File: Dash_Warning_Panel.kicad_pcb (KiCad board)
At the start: 2 copper layers, 60 x 40 mm, 30 parts, among them J1 Conn_01x06_Male, SW1 SW_DIP_x02, U1 BD2808MUV, U2 TPS22810-Q1

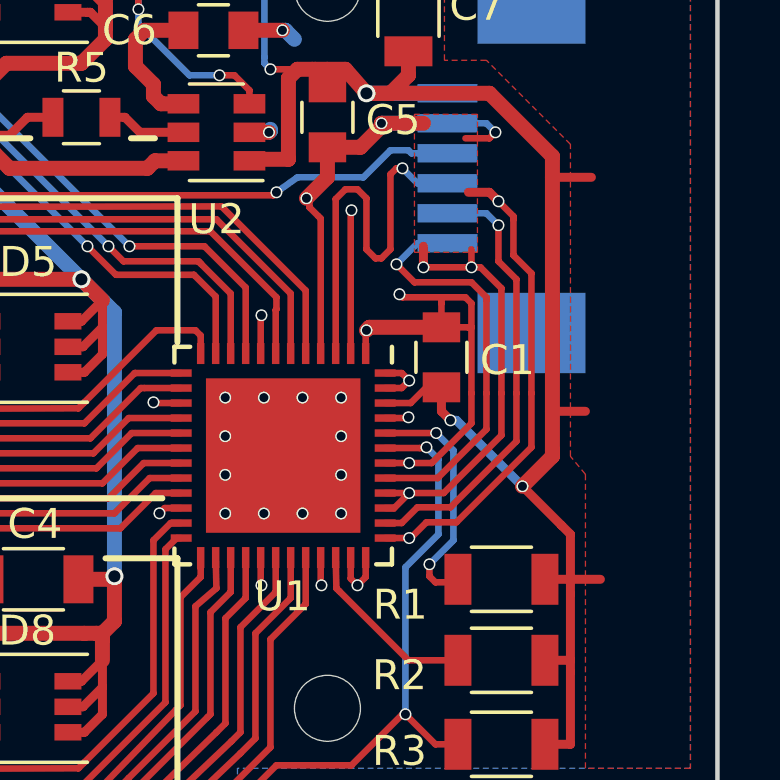
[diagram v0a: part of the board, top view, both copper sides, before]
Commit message: Fixed I2C
Address is 01111000
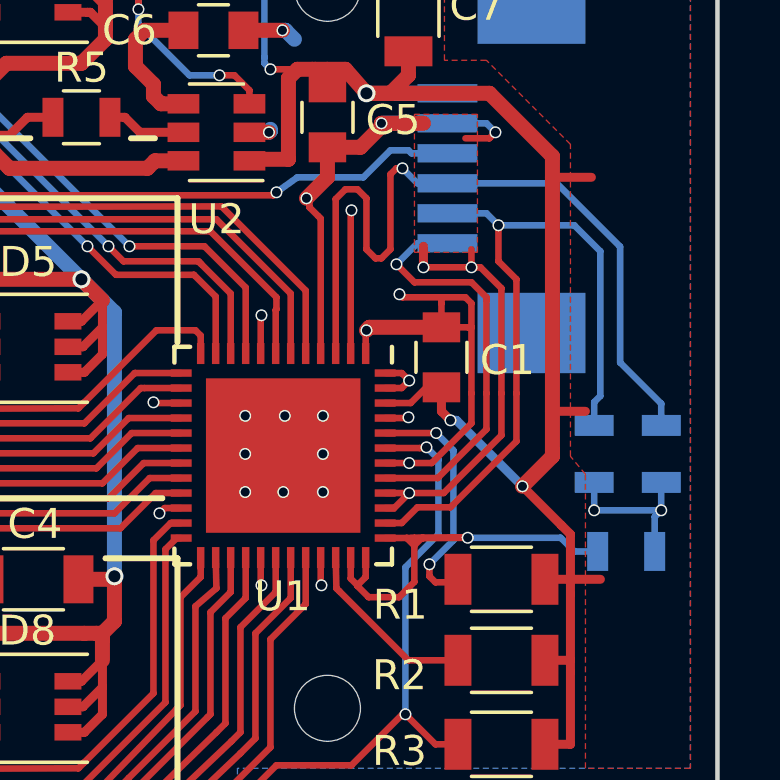
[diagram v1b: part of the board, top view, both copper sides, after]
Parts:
- added R7: 1.8k, Resistors_SMD:R_0805, B.Cu at (226.0, 134.8)
- added R8: 1.8k, Resistors_SMD:R_0805, B.Cu at (227.1, 131.5)
- added R9: 1.8k, Resistors_SMD:R_0805, B.Cu at (224.9, 131.5)
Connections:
- J1 pad : /GND -> (no net)
- U1 pad 35: /GND -> Net-(R7-Pad1)
- U1 pad 36: /GND -> Net-(R7-Pad1)
- U1 pad 37: /GND -> Net-(R7-Pad1)
- U1 pad 49: /GND -> (no net)
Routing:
- net /GND: track 83.9 -> 65.7 mm, vias 38 -> 23
- net Net-(R7-Pad1): track 0.00 -> 15.7 mm, vias 0 -> 1
- net /SDO: track 13.9 -> 27.0 mm
- net /SDI: track 14.8 -> 24.5 mm
- net /VCC: track 58.1 -> 63.6 mm, vias 5 -> 7
- net (no net): vias 0 -> 8
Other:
- board text added: "VCC GND MC SDO SDI CLK"

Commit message: LP5024
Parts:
- removed R2: 68k, Resistors_SMD:R_1206
- added C8: 1uF, Capacitors_SMD:C_0805, F.Cu at (219.2, 131.4)
- R1: value 68k -> 2.45k
- R7, R8, R9: moved to F.Cu
- REF** (x4): value 2.2mm_M2 -> MountingHole_2.2mm_M2
- U1: value BD2808MUV -> LP5024; footprint Housings_DFN_QFN:QFN-48-1EP_7x7mm_Pitch0.5mm -> TI_Additions:VQFN-32-1EP_4x4mm_Pitch0.4mm
- moved R3 4.77 mm to (219.2, 137.2)
- moved R1 4.00 mm to (221.7, 131.7), turned to 270 degrees
- moved C1 3.69 mm to (217.4, 125.5), turned to 270 degrees
- moved U1 1.58 mm to (214.7, 130.0)
- turned R8 to 90 degrees
- turned R9 to 90 degrees
- turned REF** to 0 degrees
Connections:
- C1 pad 1: /VCC -> /GND
- C1 pad 2: /GND -> Net-(C1-Pad2)
- J1 pad 1: /VCC -> /CLK
- J1 pad 2: /GND -> /SDI
- J1 pad 3: /MC -> /SDO
- J1 pad 4: /SDO -> /MC
- J1 pad 5: /SDI -> /GND
- J1 pad 6: /CLK -> /VCC
- R1 pad 2: /VCC -> /GND
- R8 pad 1: /SDO -> /CLK
- U1 pad 1: /GND -> /R0
- U1 pad 10: /G1 -> /R3
- U1 pad 11: /B1 -> /G3
- U1 pad 12: /R2 -> /B3
- U1 pad 13: /G2 -> /R4
- U1 pad 14: /B2 -> /G4
- U1 pad 15: /GND -> /B4
- U1 pad 16: /R3 -> /R5
- U1 pad 17: /G3 -> /G5
- U1 pad 18: /B3 -> /B5
- U1 pad 19: /R4 -> /R6
- U1 pad 2: /GND -> /G0
- U1 pad 20: /G4 -> /G6
- U1 pad 21: /B4 -> /B6
- U1 pad 22: /GND -> /R7
- U1 pad 23: /R5 -> /G7
- U1 pad 24: /G5 -> /B7
- U1 pad 25: /B5 -> Net-(R7-Pad1)
- U1 pad 26: /R6 -> Net-(R7-Pad1)
- U1 pad 27: /G6 -> /VCC
- U1 pad 28: /B6 -> /SDI
- U1 pad 29: /GND -> /CLK
- U1 pad 3: /SDO -> /B0
- U1 pad 30: /R7 -> /OE
- U1 pad 31: /G7 -> Net-(R1-Pad1)
- U1 pad 32: /B7 -> Net-(C1-Pad2)
- U1 pad 4: /GND -> /R1
- U1 pad 5: /R0 -> /G1
- U1 pad 6: /G0 -> /B1
- U1 pad 7: /B0 -> /R2
- U1 pad 8: /GND -> /G2
- U1 pad 9: /R1 -> /B2
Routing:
- net /VCC: track 63.6 -> 0.55 mm, vias 7 -> 0
- net /GND: track 65.7 -> 3.94 mm, vias 23 -> 4
- net /SDO: track 27.0 -> 0.00 mm, vias 1 -> 0
- net /SDI: track 24.5 -> 0.55 mm, vias 1 -> 0
- net Net-(R7-Pad1): track 15.7 -> 1.10 mm, vias 1 -> 0
- net /CLK: track 13.9 -> 0.55 mm, vias 1 -> 0
- net /OE: track 85.5 -> 74.2 mm, vias 3 -> 1
- net Net-(R1-Pad1): track 8.12 -> 0.55 mm, vias 2 -> 0
- net /MC: track 38.7 -> 32.4 mm
- net Net-(R2-Pad2): track 6.07 -> 0.00 mm
- net /G2: track 35.2 -> 39.6 mm
- net /G6: track 31.7 -> 35.5 mm
- net /R6: track 30.8 -> 34.5 mm
- net /B6: track 35.9 -> 39.5 mm
- net /B5: track 44.3 -> 47.8 mm
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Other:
- net class Default: clearance 0.15 -> 0.18
- rule trace_clearance: 0.15 -> 0.18
- rule trace_min: 0.2 -> 0.16

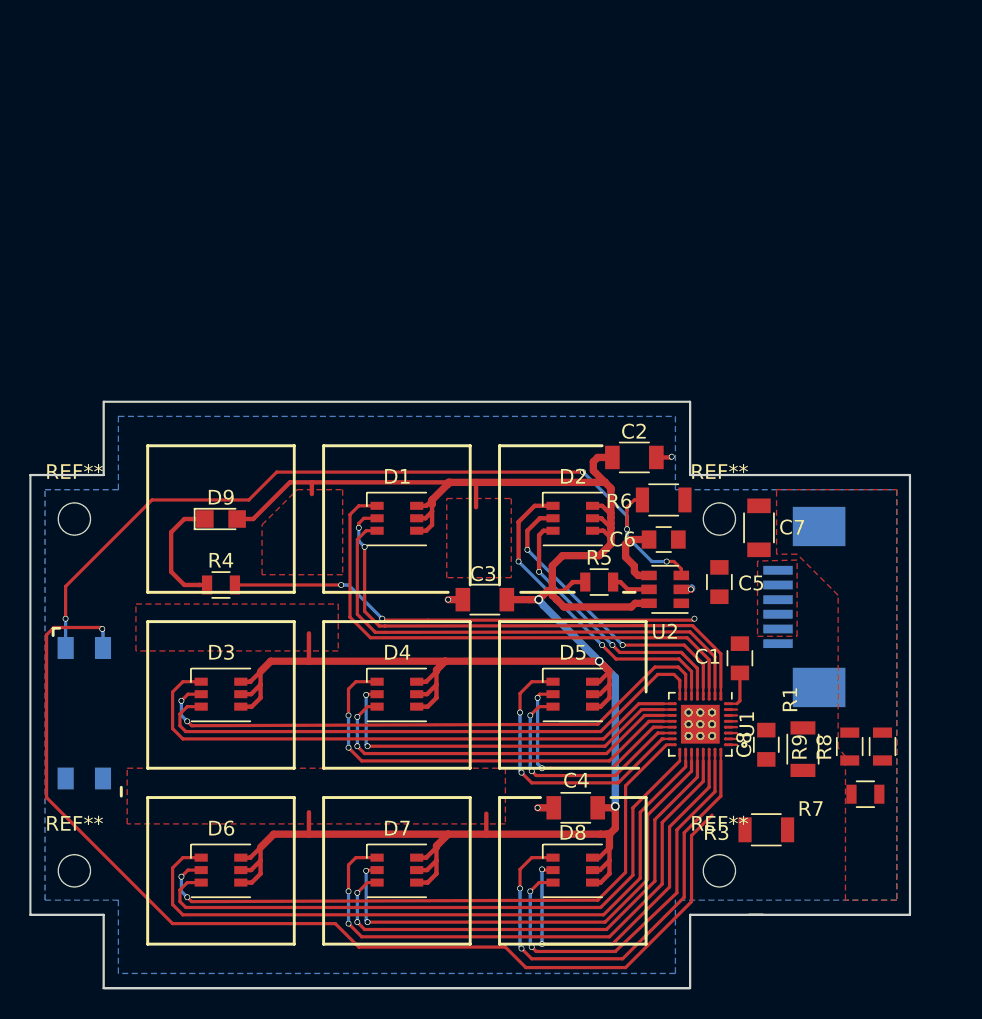
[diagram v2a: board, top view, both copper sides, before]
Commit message: Routing with LP5024
Ready for Fabrication Review
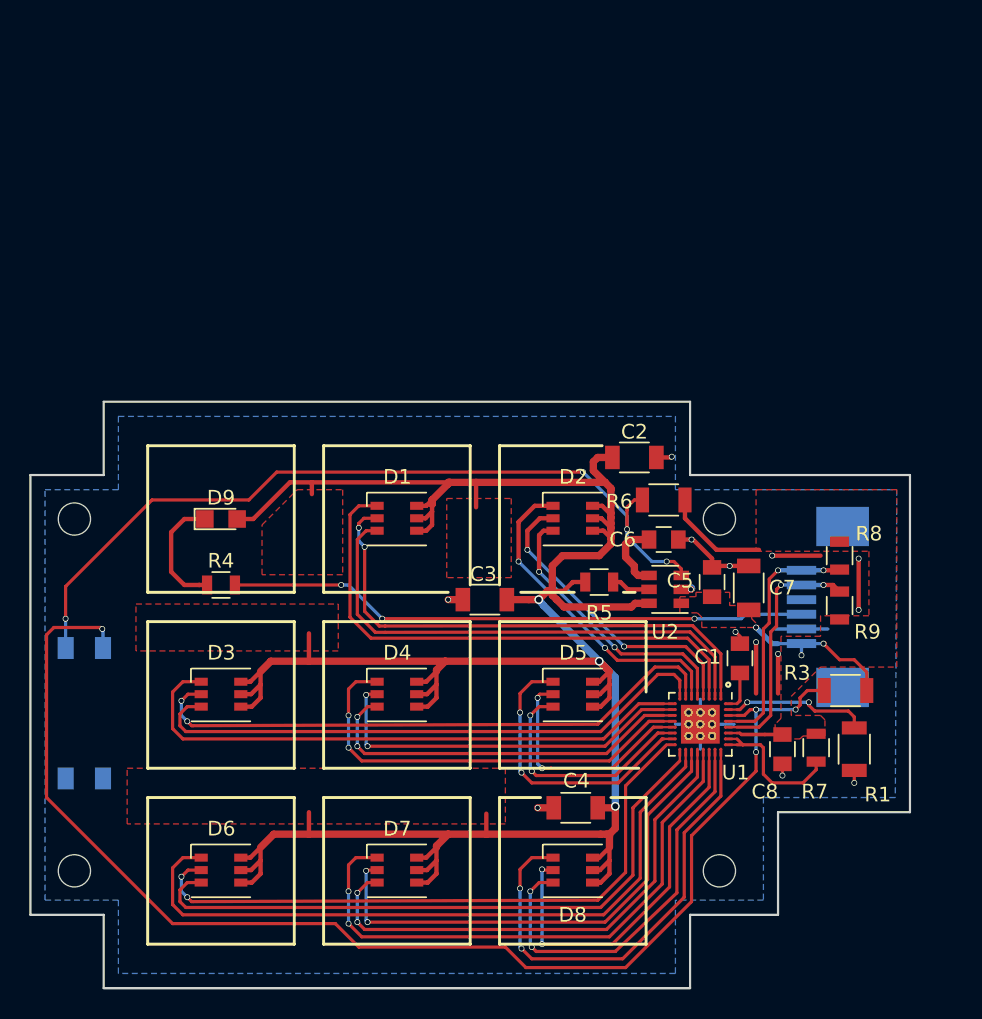
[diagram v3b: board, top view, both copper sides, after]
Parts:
- moved R8 13.3 mm to (224.2, 118.5)
- moved R3 10.9 mm to (224.6, 127.7)
- moved R9 9.65 mm to (224.2, 121.9), turned to 270 degrees
- moved R7 4.62 mm to (222.6, 131.6), turned to 90 degrees
- moved C7 4.16 mm to (218.0, 120.7)
- moved R1 3.50 mm to (225.2, 131.7)
- moved J1 1.60 mm to (223.4, 122.0)
- moved C8 1.14 mm to (220.3, 131.7)
- moved C5 0.50 mm to (215.5, 120.3), turned to 270 degrees
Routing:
- net /GND: track 3.94 -> 41.1 mm, vias 4 -> 14
- net /VCC: track 0.55 -> 22.1 mm, vias 0 -> 3
- net /CLK: track 0.55 -> 16.9 mm, vias 0 -> 2
- net /SDI: track 0.55 -> 16.6 mm, vias 0 -> 2
- net /OE: track 74.2 -> 89.6 mm, vias 1 -> 4
- net Net-(R1-Pad1): track 0.55 -> 10.0 mm, vias 0 -> 2
- net Net-(R7-Pad1): track 1.10 -> 10.2 mm
- net /MC: track 32.4 -> 39.7 mm
- removed copper zone on F.Cu, net /GND
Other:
- outline, holes or cut-outs redrawn
- net class Default: clearance 0.18 -> 0.17
- rule trace_clearance: 0.18 -> 0.17
- board text added: "CLK SDI SDO MC GND VCC"
- board text added: "Drive On"
- board text added: "Power On"
- board text removed: "VCC GND MC SDO SDI CLK"

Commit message: 2020 Warning Panel Design
Added Green 7 Segment Display driven by shift driver
Light 1 changed to Neutral Engage Direct driven diode off 5V power system
Light 2-9 all off of shift driver
Standardized LEDs and resistors with main panel
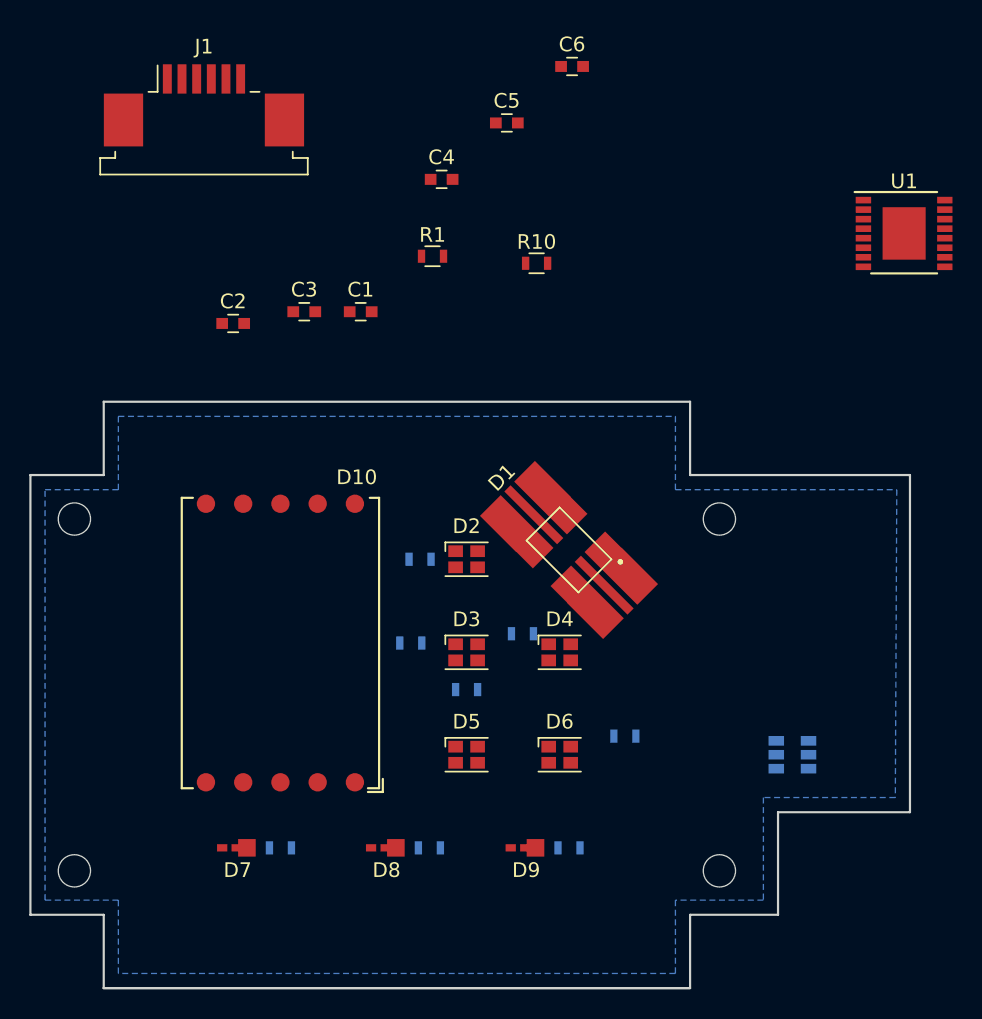
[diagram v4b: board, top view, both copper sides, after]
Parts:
- removed C7: 4.7uF, Capacitors_SMD:C_1206
- removed C8: 1uF, Capacitors_SMD:C_0805
- removed SW1: SW_DIP_x02, Apem:2.54mm_DIP_Switch_2_Position
- added D10: DSM7T, VCC:DSM77TA56105T, F.Cu at (186.1, 124.5)
- added R10: 86.6, Resistors_SMD:R_0603, F.Cu at (203.5, 98.6)
- added R2: 71, Resistors_SMD:R_0603, B.Cu at (195.6, 118.7)
- C1, C5, C6: footprint Capacitors_SMD:C_0805 -> Capacitors_SMD:C_0603
- C2, C3, C4: value 4.7uF -> 1uF; footprint Capacitors_SMD:C_1206 -> Capacitors_SMD:C_0603
- D1: value LED_RGB_Wurth -> LCB G6SP; footprint Wurth:LED_RGB_3528 -> OSRAM:PLCC-6_THERM_MOD
- D2, D6: value LED_RGB_Wurth -> LY E6SF; footprint Wurth:LED_RGB_3528 -> LEDs:LED_Cree-PLCC4_2x2mm_CW
- D3, D4, D5: value LED_RGB_Wurth -> LS E6SF; footprint Wurth:LED_RGB_3528 -> LEDs:LED_Cree-PLCC4_2x2mm_CW
- D7, D8: value LED_RGB_Wurth -> KP DELPS; footprint Wurth:LED_RGB_3528 -> OSRAM:PLCC-2
- D9: value LED -> KP DELPS; footprint LEDs:LED_0805 -> OSRAM:PLCC-2
- J1: value Conn_01x06_Male -> Conn; moved to F.Cu
- R1: value 2.45k -> 11.3; footprint Resistors_SMD:R_1206 -> Resistors_SMD:R_0603
- R3, R6: value 68k -> 71; footprint Resistors_SMD:R_1206 -> Resistors_SMD:R_0603; moved to B.Cu
- R4, R5: value 86.6 -> 71; footprint Resistors_SMD:R_0805 -> Resistors_SMD:R_0603; moved to B.Cu
- R7, R8, R9: value 1.8k -> 116.7; footprint Resistors_SMD:R_0805 -> Resistors_SMD:R_0603; moved to B.Cu
- U1: value LP5024 -> TLC6C598; footprint TI_Additions:VQFN-32-1EP_4x4mm_Pitch0.4mm -> Housings_SSOP:TSSOP-16-1EP_4.4x5mm_Pitch0.65mm
- U2: value TPS22810-Q1 -> TPS22810; moved to B.Cu
- moved J1 54.6 mm to (180.8, 87.8), turned to 0 degrees
- moved R1 44.3 mm to (196.4, 98.1), turned to 0 degrees
- moved C4 43.8 mm to (197.1, 92.8), turned to 0 degrees
- moved R7 37.2 mm to (186.1, 138.4), turned to 0 degrees
- moved U1 36.3 mm to (228.6, 96.5), turned to 0 degrees
- moved C1 35.0 mm to (191.5, 101.9), turned to 0 degrees
- moved R8 34.4 mm to (196.2, 138.4), turned to 0 degrees
- moved C5 34.3 mm to (201.5, 89.0), turned to 0 degrees
- moved C6 32.9 mm to (206.0, 85.1), turned to 0 degrees
- moved D9 30.0 mm to (201.9, 138.4)
- moved R3 29.8 mm to (194.9, 124.5)
- moved C2 28.9 mm to (182.8, 102.7)
- moved R9 24.8 mm to (205.7, 138.4), turned to 0 degrees
- moved D6 24.4 mm to (205.1, 132.1)
- moved C3 23.2 mm to (187.7, 101.9), turned to 0 degrees
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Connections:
- C1 pad 1: /GND -> /VCC
- C1 pad 2: Net-(C1-Pad2) -> /GND
- C2 pad 2: /GND -> Net-(C2-Pad2)
- C3 pad 2: /GND -> Net-(C2-Pad2)
- C4 pad 2: /GND -> Net-(C2-Pad2)
- C5 pad 1: /GND -> Net-(C2-Pad2)
- C6 pad 1: /GND -> Net-(C2-Pad2)
- D1 pad 1: /B0 -> Net-(D1-Pad1)
- D1 pad 2: /LED_Power -> Net-(D1-Pad2)
- D2 pad 1: /B1 -> Net-(D2-Pad1)
- D2 pad 2: /LED_Power -> Net-(D2-Pad2)
- D2 pad 3: /R1 -> (no net)
- D2 pad 4: /LED_Power -> (no net)
- D3 pad 1: /B2 -> Net-(D3-Pad1)
- D3 pad 2: /LED_Power -> Net-(D3-Pad2)
- D3 pad 3: /R2 -> (no net)
- D3 pad 4: /LED_Power -> (no net)
- D4 pad 1: /B3 -> Net-(D4-Pad1)
- D4 pad 2: /LED_Power -> Net-(D4-Pad2)
- D4 pad 3: /R3 -> (no net)
- D4 pad 4: /LED_Power -> (no net)
- D5 pad 1: /B4 -> Net-(D5-Pad1)
- D5 pad 2: /LED_Power -> Net-(D5-Pad2)
- D5 pad 3: /R4 -> (no net)
- D5 pad 4: /LED_Power -> (no net)
- D6 pad 1: /B5 -> Net-(D6-Pad1)
- D6 pad 2: /LED_Power -> Net-(D6-Pad2)
- D6 pad 3: /R5 -> (no net)
- D6 pad 4: /LED_Power -> (no net)
- D7 pad 2: /LED_Power -> Net-(D7-Pad2)
- D7 pad 3: /R6 -> (no net)
- D8 pad 2: /LED_Power -> Net-(D8-Pad2)
- D8 pad 3: /R7 -> (no net)
- D9 pad 2: /LED_Power -> Net-(D9-Pad2)
- J1 pad 1: /CLK -> /VCC
- J1 pad 2: /SDI -> /GND
- J1 pad 3: /SDO -> /NEUT
- J1 pad 4: /MC -> /SDI
- J1 pad 5: /GND -> /SCLK
- J1 pad 6: /VCC -> /RCLK
- R1 pad 1: Net-(R1-Pad1) -> Net-(D1-Pad1)
- R1 pad 2: /GND -> /NEUT
- R3 pad 1: /OE -> Net-(D3-Pad1)
- R3 pad 2: /VCC -> Net-(R3-Pad2)
- R4 pad 1: Net-(D9-Pad1) -> Net-(D4-Pad1)
- R4 pad 2: /MC -> Net-(R4-Pad2)
- R5 pad 1: /LED_Power -> Net-(D5-Pad1)
- R6 pad 1: /VCC -> Net-(D6-Pad1)
- R6 pad 2: /EN -> Net-(R6-Pad2)
- R7 pad 1: Net-(R7-Pad1) -> Net-(D7-Pad1)
- R7 pad 2: /VCC -> Net-(R7-Pad2)
- R8 pad 1: /CLK -> Net-(D8-Pad1)
- R8 pad 2: /VCC -> Net-(R8-Pad2)
- R9 pad 1: /SDI -> Net-(D9-Pad1)
- R9 pad 2: /VCC -> Net-(R9-Pad2)
- U1 pad 1: /R0 -> Net-(U1-Pad1)
- U1 pad 10: /R3 -> Net-(U1-Pad10)
- U1 pad 11: /G3 -> Net-(U1-Pad11)
- U1 pad 12: /B3 -> Net-(U1-Pad12)
- U1 pad 13: /R4 -> Net-(U1-Pad13)
- U1 pad 14: /G4 -> Net-(U1-Pad14)
- U1 pad 15: /B4 -> Net-(U1-Pad15)
- U1 pad 16: /R5 -> Net-(U1-Pad16)
- U1 pad 17: /G5 -> (no net)
- U1 pad 2: /G0 -> Net-(U1-Pad2)
- U1 pad 3: /B0 -> Net-(U1-Pad3)
- U1 pad 4: /R1 -> Net-(U1-Pad4)
- U1 pad 5: /G1 -> Net-(U1-Pad5)
- U1 pad 6: /B1 -> Net-(U1-Pad6)
- U1 pad 7: /R2 -> Net-(U1-Pad7)
- U1 pad 8: /G2 -> Net-(U1-Pad8)
- U1 pad 9: /B2 -> Net-(U1-Pad9)
- U2 pad 2: /GND -> Net-(C2-Pad2)
- U2 pad 3: /EN -> /VCC
- U2 pad 5: Net-(R5-Pad2) -> Net-(R10-Pad2)
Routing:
- net /LED_Power: track 180.8 -> 0.00 mm, vias 3 -> 0
- net /OE: track 89.6 -> 0.00 mm, vias 4 -> 0
- net /EN: track 56.2 -> 0.00 mm, vias 4 -> 0
- net /B5: track 47.8 -> 0.00 mm
- net /R5: track 44.1 -> 0.00 mm, vias 2 -> 0
- net /G5: track 44.1 -> 0.00 mm
- net /GND: track 41.1 -> 0.00 mm, vias 14 -> 0
- net /R2: track 40.5 -> 0.00 mm, vias 2 -> 0
- net /B2: track 40.1 -> 0.00 mm
- net /MC: track 39.7 -> 0.00 mm, vias 3 -> 0
- net /G2: track 39.6 -> 0.00 mm
- net /B6: track 39.5 -> 0.00 mm, vias 2 -> 0
- net /B0: track 37.2 -> 0.00 mm
- net /R0: track 35.9 -> 0.00 mm, vias 2 -> 0
- net /G6: track 35.5 -> 0.00 mm, vias 2 -> 0
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- removed copper zone on F.Cu, net /LED_Power
- removed copper zone on F.Cu, net /VCC
